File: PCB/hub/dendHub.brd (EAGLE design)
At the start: 59.7 x 47 mm, 6 parts

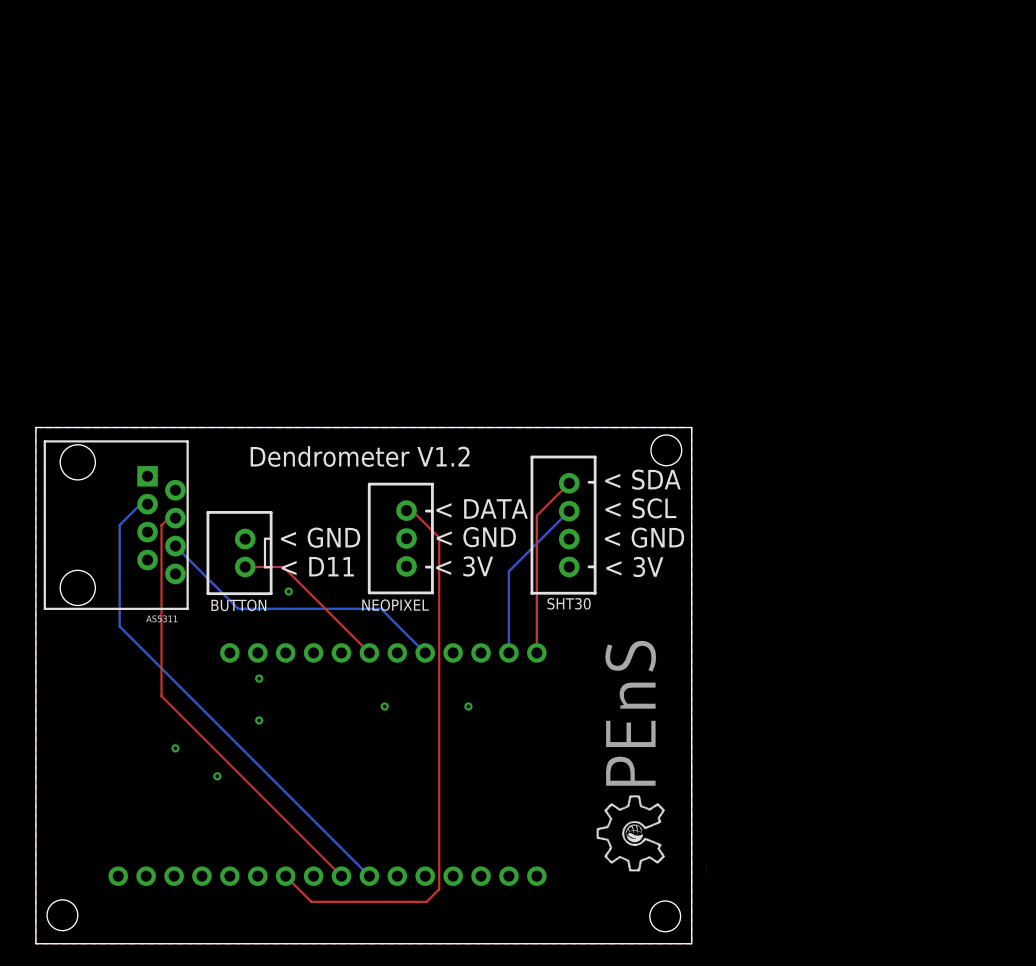
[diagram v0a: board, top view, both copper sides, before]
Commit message: Dendrometer V1.2
Updated PCBs for node and hub as well as includes code for both Ethernet and LTE telemetry
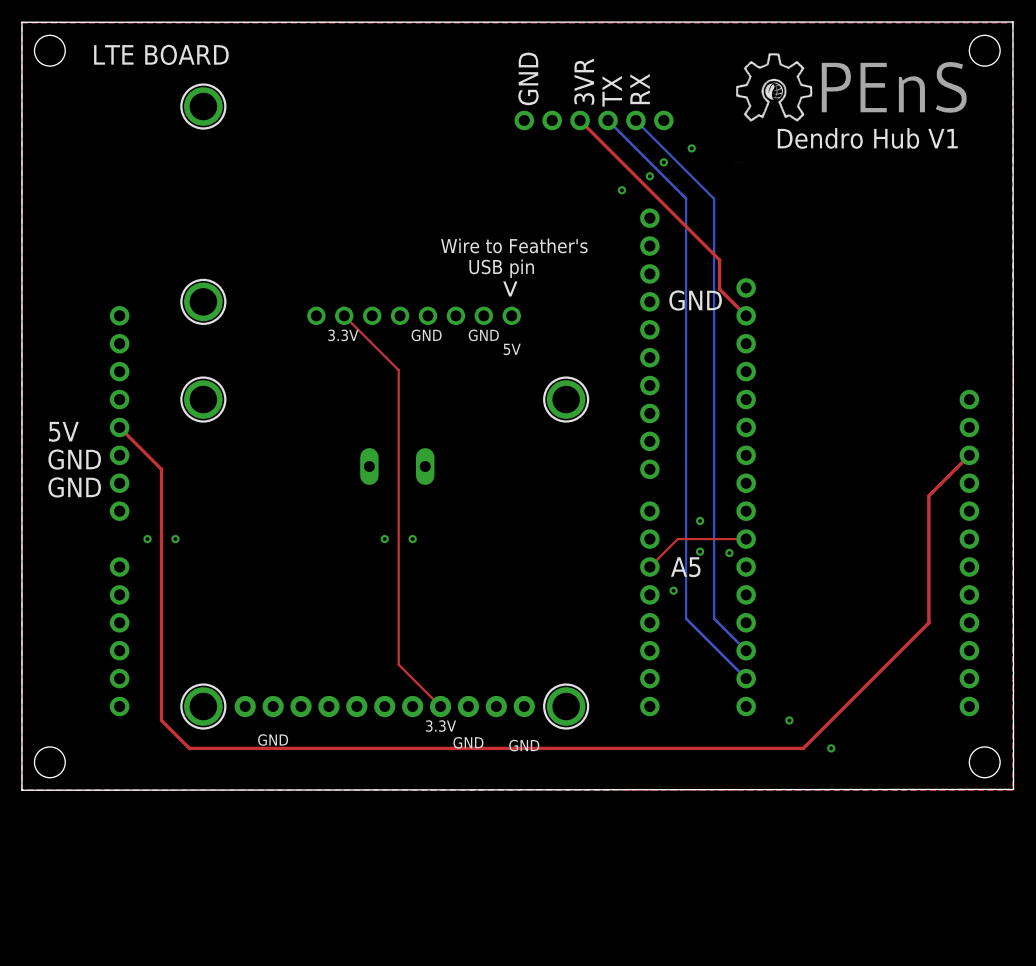
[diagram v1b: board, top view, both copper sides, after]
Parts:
- removed AS5311: RJ45, SparkFun-Connectors:RJ45-8
- removed BUTTON: JST-XH-02-PIN-ROUND-PAD, Rembrandt Electronics - JST XH Connectors v1-0:JST-XH-02-PACKAGE-ROUND-PAD
- removed NEOPIXEL: JST-XH-03-PIN-ROUND-PAD, Rembrandt Electronics - JST XH Connectors v1-0:JST-XH-03-PACKAGE-ROUND-PAD
- removed SHT30: JST-XH-04-PIN-ROUND-PAD, Rembrandt Electronics - JST XH Connectors v1-0:JST-XH-04-PACKAGE-ROUND-PAD
- added JP1: (no value), microbuilder:1X08_ROUND
- added JP11, JP12: (no value), microbuilder:1X01_OVAL
- added JP9: (no value), microbuilder:1X11_ROUND_76
- added U$2: (no value), opens-logo:OPENS-LOGO
- added U$45, U$46, U$47, U$48, U$56, U$57: MOUNTINGHOLE2.5, microbuilder:MOUNTINGHOLE_2.5_PLATED
- MS1: device modifiedAdafruit:FEATHERWING -> adafruit:FEATHERWING
- U$1: value (none) -> LTE_BOARD; device opens-logo:OPENS-LOGO -> LTE_BOARD:LTE_BOARD_FOOTPRINT
- moved MS1 87.3 mm to (63.4, 58.4), turned to 270 degrees
- moved U$1 73.7 mm to (7.62, 49.5), turned to 270 degrees
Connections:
- removed net A2: MS1.7, NEOPIXEL.3
- removed net CSN: AS5311.6, MS1.21
- removed net D11: BUTTON.1, MS1.23
- removed net DO: AS5311.4, MS1.9
- removed net SCL: MS1.18, SHT30.3
- removed net SCLK: AS5311.3, MS1.10
- removed net SDA: MS1.17, SHT30.4
- new net 5VRAIL: MS1.26, U$1.5V
- new net N$1: JP1.8
- new net PWR_ON: MS1.10, U$1.5
- new net RX: MS1.14, U$1.TX
- new net TX: MS1.15, U$1.RX
- new net VBUS: JP12.1
- new net VOUT: JP1.2, JP9.4
- net 3VRAIL: now also U$1.VIO; no longer AS5311.1, AS5311.2, NEOPIXEL.1, SHT30.1
- net GND: now also JP1.5, JP1.7, JP11.1, JP9.1, JP9.10, JP9.3, U$1.GND, U$1.GND1, U$1.GND2, U$1.GND3; no longer AS5311.5, BUTTON.2, NEOPIXEL.2, SHT30.2
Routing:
- net 5VRAIL: track 0.00 -> 120.7 mm
- net TX: track 0.00 -> 56.0 mm
- net RX: track 0.00 -> 52.4 mm
- net A2: track 51.4 -> 0.00 mm
- net SCLK: track 44.7 -> 0.00 mm
- net DO: track 40.3 -> 0.00 mm
- net VOUT: track 0.00 -> 39.2 mm
- net CSN: track 26.8 -> 0.00 mm
- net 3VRAIL: track 0.00 -> 24.0 mm, vias 3 -> 0
- net SDA: track 16.7 -> 0.00 mm
- net SCL: track 15.2 -> 0.00 mm
- net D11: track 14.5 -> 0.00 mm
- net PWR_ON: track 0.00 -> 9.82 mm
- added copper zone on layer 16, net GND
- removed copper zone on layer 16, net 3VRAIL
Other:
- board size 59.7 x 47 mm -> 90.3 x 69.9 mm
- board text added: "3.3V"
- board text added: "3VR"
- board text added: "5V"
- board text added: "<"
- board text added: "A5"
- board text added: "Dendro Hub V1"
- board text added: "GND"
- board text added: "Hypnos V3.1"
- board text added: "LTE BOARD"
- board text added: "POWERBOOST"
- board text added: "RX"
- board text added: "SOLAR CHARGER"
- board text added: "TX"
- board text added: "Units in inches"
- board text added: "Wire to Feather's USB pin"
- board text removed: "< 3V"
- board text removed: "< D11"
- board text removed: "< DATA"
- board text removed: "< GND"
- board text removed: "< SCL"
- board text removed: "< SDA"
- board text removed: "Dendrometer V1.2"

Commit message: Summer 2022 Deployment Prep
Updated PCBs and code, includes Loom V3 and HypnosV3.3 changes
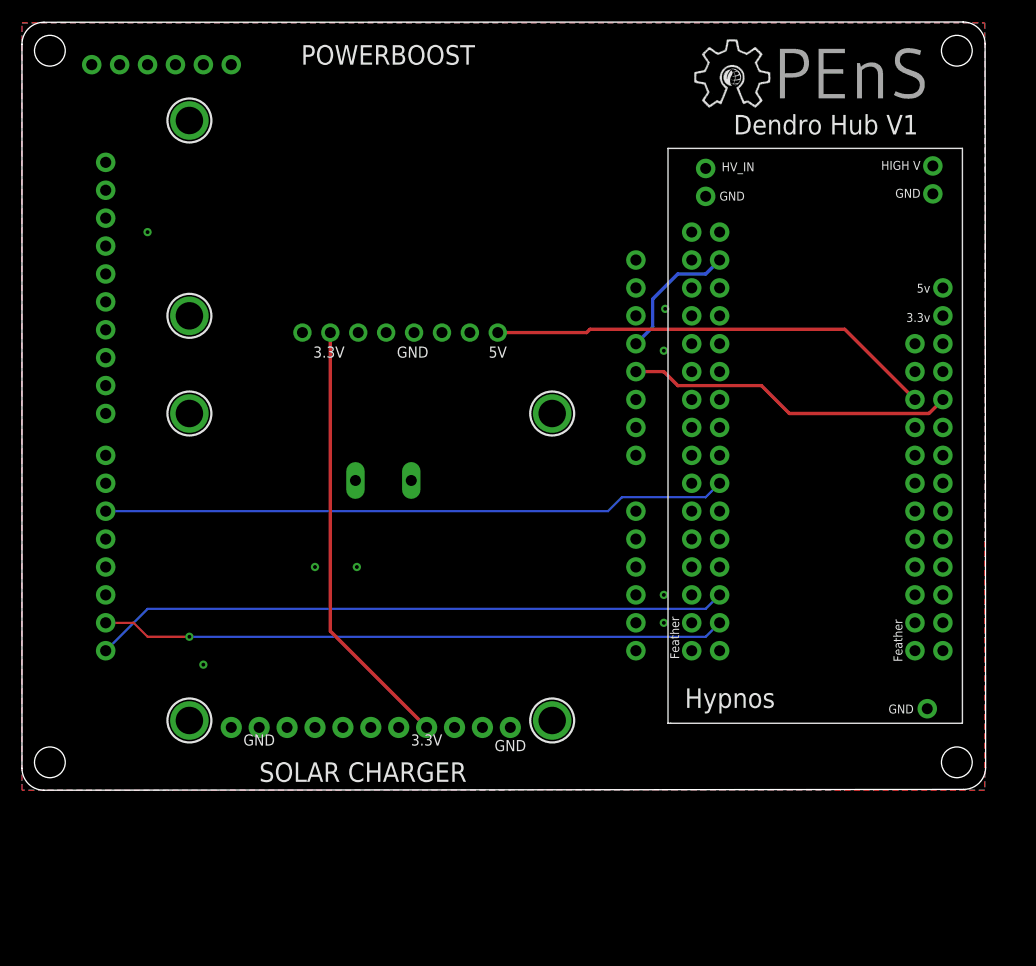
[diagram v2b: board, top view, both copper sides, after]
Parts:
- removed MS1: FEATHERWING, adafruit:FEATHERWING
- added U$3: HYPNOS_V3, HYPNOS_V3:HYPNOS_V3
- moved U$1 47.3 mm to (54.6, 54.6), flipped to the bottom
- moved U$2 4.02 mm to (59.7, 64.8)
- moved JP9 2.29 mm to (30.5, 12.1)
- moved JP1 1.98 mm to (33.1, 48.0)
- moved JP11 1.80 mm to (34.2, 34.5)
- moved JP12 1.80 mm to (29.1, 34.5)
- moved U$45 1.80 mm to (14.0, 12.7)
- moved U$48 1.80 mm to (47.0, 12.7)
- moved U$46 1.80 mm to (14.0, 40.6)
- moved U$56 1.80 mm to (14.0, 67.3)
- moved U$57 1.80 mm to (14.0, 49.5)
- moved U$47 1.80 mm to (47.0, 40.6)
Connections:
- net 3VRAIL: now also U$1.3.3V, U$3.3VRAIL; no longer MS1.2, U$1.VIO
- net 5VRAIL: now also U$3.5VRAIL; no longer MS1.26
- net GND: now also U$3.GND, U$3.GND4; no longer MS1.4, U$1.GND, U$1.GND2
- net N$1: now also U$3.5VUSB
- net PWR_ON: now also U$3.A51; no longer MS1.10
- net RX: now also U$1.0, U$3.RX1; no longer MS1.14, U$1.TX
- net TX: now also U$1.1, U$3.TX1; no longer MS1.15, U$1.RX
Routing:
- net 5VRAIL: track 120.7 -> 30.0 mm
- net PWR_ON: track 9.82 -> 56.9 mm
- net N$1: track 0.00 -> 40.8 mm
- net 3VRAIL: track 24.0 -> 12.3 mm
- net RX: track 52.4 -> 58.0 mm
- net TX: track 56.0 -> 56.9 mm, vias 0 -> 1
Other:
- board size 90.3 x 69.9 mm -> 87.7 x 69.9 mm
- board text added: "3V"
- board text added: "Rx"
- board text added: "Tx\"
- board text removed: "3VR"
- board text removed: "<"
- board text removed: "RX"
- board text removed: "TX"
- board text removed: "Wire to Feather's USB pin"
